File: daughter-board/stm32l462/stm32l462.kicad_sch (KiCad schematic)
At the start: 50 parts, among them J1 Conn_02x10_Odd_Even, J2 Conn_02x10_Odd_Even, U1 STM32L476RG, U2 STM32L462CETx, Y1 Crystal_Small

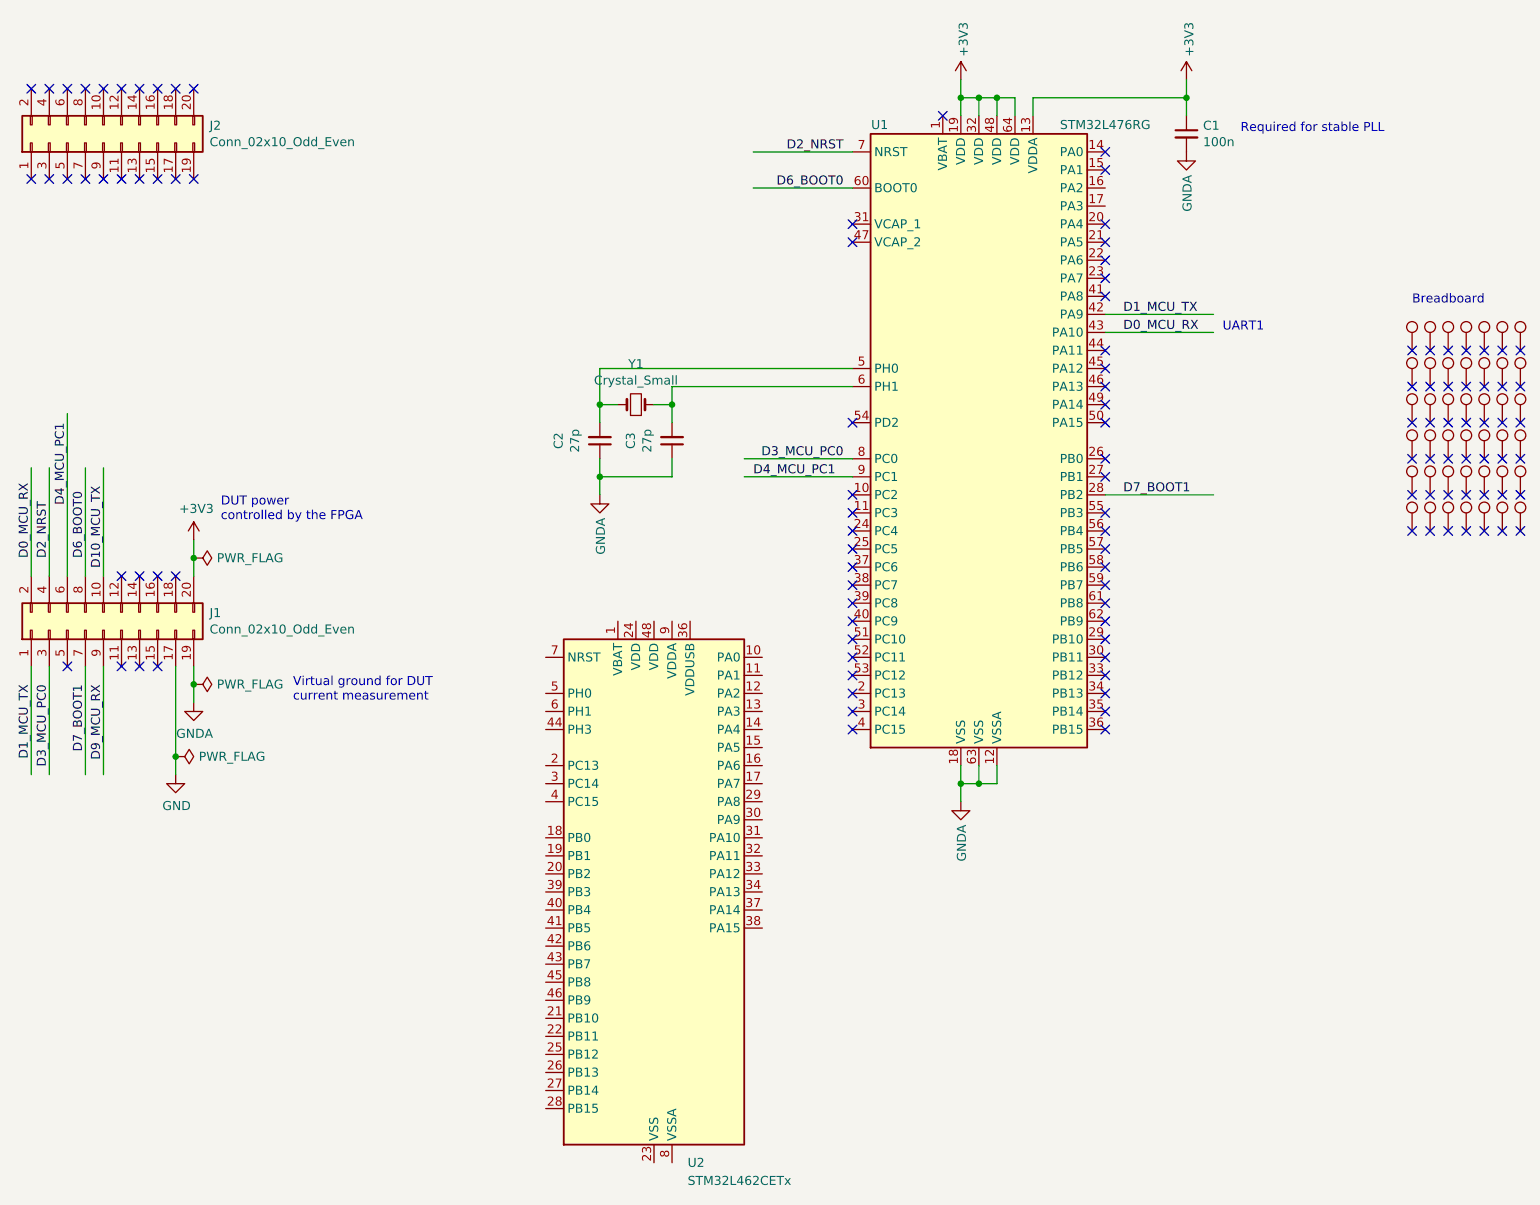
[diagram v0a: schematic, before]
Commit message: Change package folder name - Add integration test and actions script
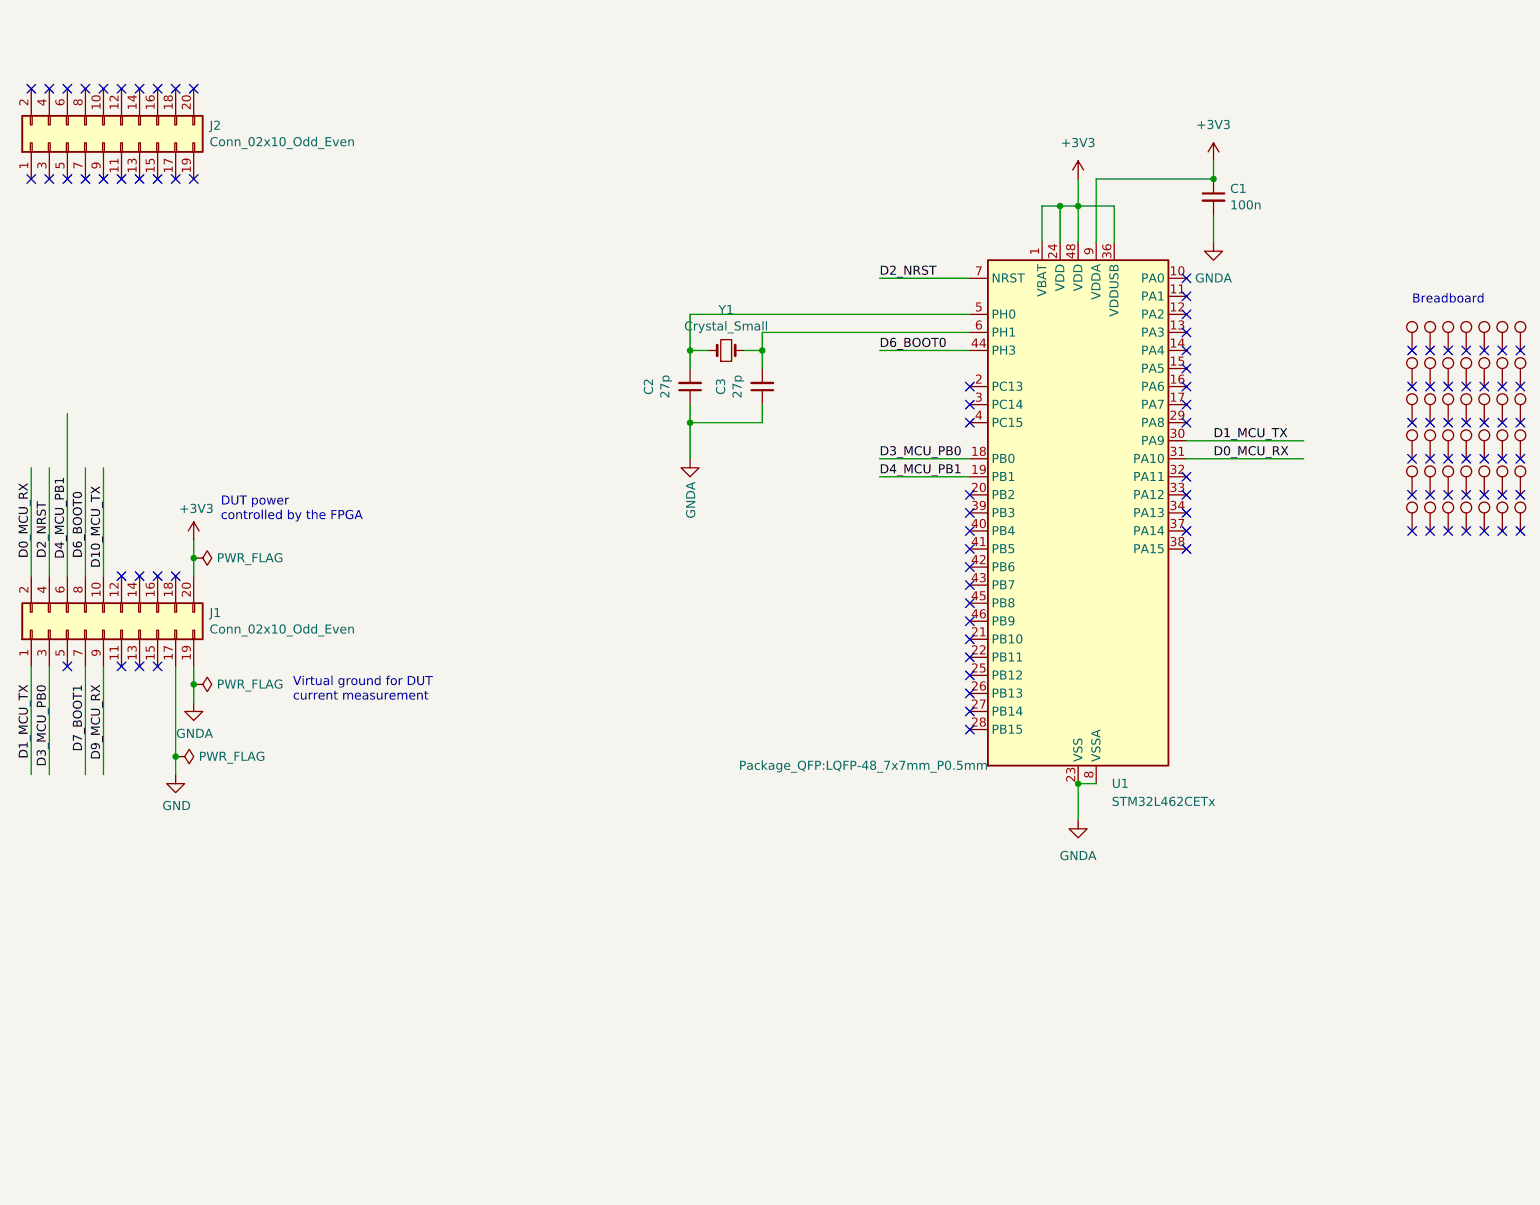
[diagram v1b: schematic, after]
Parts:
- removed U1: STM32L476RG, mykicadlibs:ALLSOCKET-QFP64, symbol stm32f205-rescue:STM32F205RETx-MCU_ST_STM32F2
- renumbered U2 to U1
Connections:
- net D3_MCU_PC0 is gone; now on net D3_MCU_PB0: J1.3 (Pin_3)
- net D4_MCU_PC1 is gone; now on net D4_MCU_PB1: J1.6 (Pin_6)
- net +3V3: now also U1.1 (VBAT), U1.24 (VDD), U1.36 (VDDUSB), U1.48 (VDD), U1.9 (VDDA)
- net D0_MCU_RX: now also U1.31 (PA10)
- net D1_MCU_TX: now also U1.30 (PA9)
- net D2_NRST: now also U1.7 (NRST)
- net D6_BOOT0: now also U1.44 (PH3)
- net GNDA: now also U1.23 (VSS), U1.35 (VSS), U1.47 (VSS), U1.8 (VSSA)
- net at C2.2, Y1.1: now also U1.5 (PH0)
- net at C3.2, Y1.2: now also U1.6 (PH1)
- net D3_MCU_PB0: now reaches U1.18 (PB0)
- net D4_MCU_PB1: now reaches U1.19 (PB1)
- no-connect marks 115 -> 101
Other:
- note removed: "Required for stable PLL"
- note removed: "UART1"
- title: Scaffold STM32L476 daughterboard -> Scaffold STM32L462aughterboard
- moved on the sheet: C2, C3, U1, Y1
